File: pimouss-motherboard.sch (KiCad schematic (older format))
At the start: 0 parts

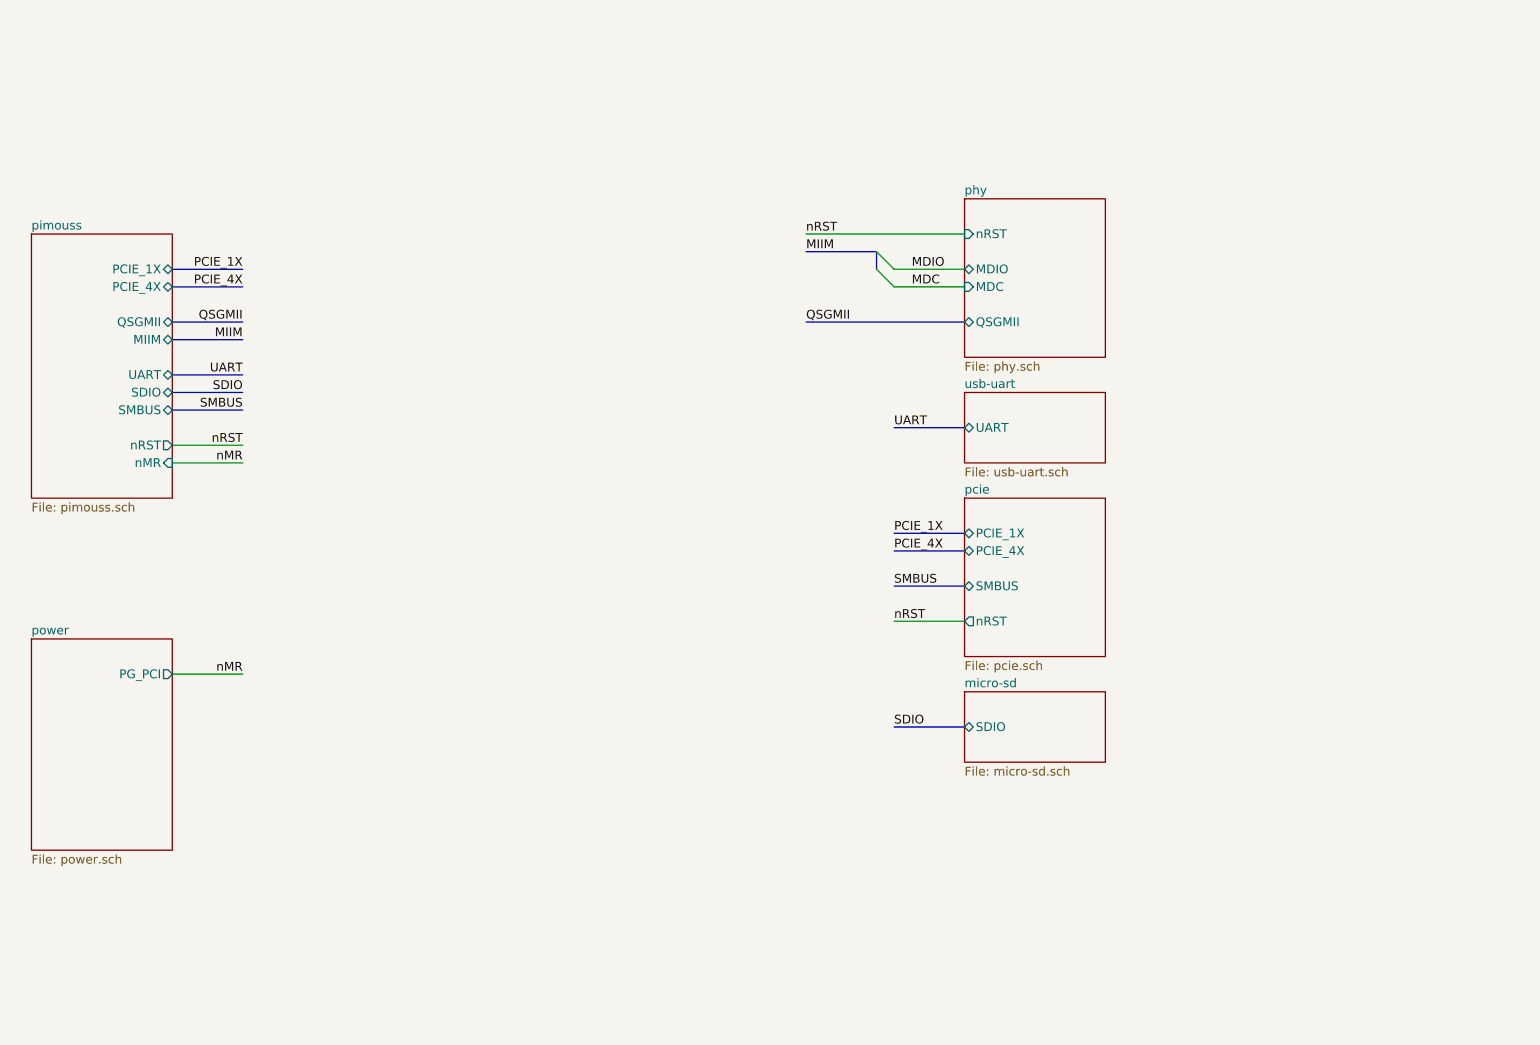
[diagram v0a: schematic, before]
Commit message: sch: Move PHY blocks to main page
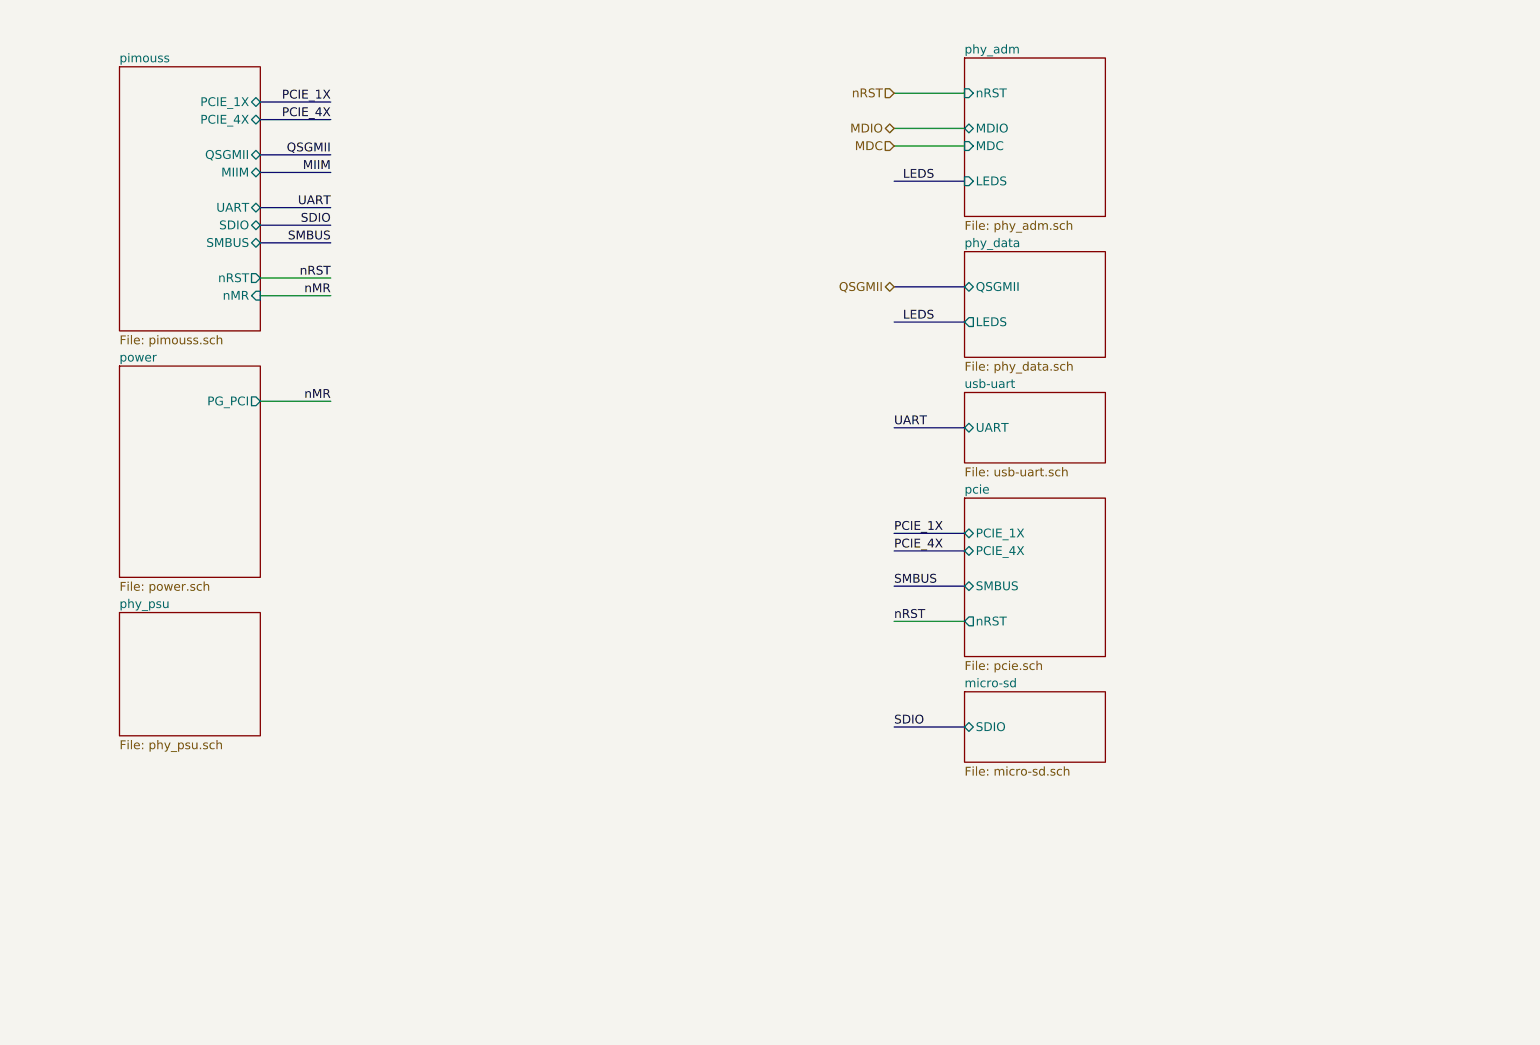
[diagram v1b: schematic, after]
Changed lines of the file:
@@
 $Descr A4 11693 8268
 encoding utf-8
-Sheet 1 13
+Sheet 1 12
 Title "Global motherboard interconnections"
 Date "2019-03-19"
@@
 $EndDescr
 $Sheet
-S 2100 2400 800  1500
+S 2600 1450 800  1500
 U 5CE77C37
 F0 "pimouss" 50
 F1 "pimouss.sch" 50
-F2 "PCIE_1X" B R 2900 2600 50
-F3 "PCIE_4X" B R 2900 2700 50
-F4 "QSGMII" B R 2900 2900 50
-F5 "MIIM" B R 2900 3000 50
-F6 "UART" B R 2900 3200 50
-F7 "SDIO" B R 2900 3300 50
-F8 "SMBUS" B R 2900 3400 50
-F9 "nRST" O R 2900 3600 50
-F10 "nMR" I R 2900 3700 50
-$EndSheet
-$Sheet
-S 7400 2200 800  900
-U 5C7D0D1E
-F0 "phy" 50
-F1 "phy.sch" 50
-F2 "nRST" I L 7400 2400 50
-F3 "MDIO" B L 7400 2600 50
-F4 "MDC" I L 7400 2700 50
-F5 "QSGMII" B L 7400 2900 50
+F2 "PCIE_1X" B R 3400 1650 50
+F3 "PCIE_4X" B R 3400 1750 50
+F4 "QSGMII" B R 3400 1950 50
+F5 "MIIM" B R 3400 2050 50
+F6 "UART" B R 3400 2250 50
+F7 "SDIO" B R 3400 2350 50
+F8 "SMBUS" B R 3400 2450 50
+F9 "nRST" O R 3400 2650 50
+F10 "nMR" I R 3400 2750 50
 $EndSheet
 Wire Bus Line
-	2900 2600 3300 2600
-Text Label 3300 2600 2    50   ~ 0
+	3400 1650 3800 1650
+Text Label 3800 1650 2    50   ~ 0
 PCIE_1X
 Wire Bus Line
-	2900 2700 3300 2700
-Text Label 3300 2700 2    50   ~ 0
+	3400 1750 3800 1750
+Text Label 3800 1750 2    50   ~ 0
 PCIE_4X
 Wire Bus Line
-	2900 2900 3300 2900
-Text Label 3300 2900 2    50   ~ 0
+	3400 1950 3800 1950
+Text Label 3800 1950 2    50   ~ 0
 QSGMII
 Wire Bus Line
-	3300 3000 2900 3000
-Text Label 3300 3000 2    50   ~ 0
+	3800 2050 3400 2050
+Text Label 3800 2050 2    50   ~ 0
 MIIM
 Wire Bus Line
-	2900 3200 3300 3200
-Text Label 3300 3200 2    50   ~ 0
+	3400 2250 3800 2250
+Text Label 3800 2250 2    50   ~ 0
 UART
 Wire Bus Line
-	2900 3300 3300 3300
-Text Label 3300 3300 2    50   ~ 0
+	3400 2350 3800 2350
+Text Label 3800 2350 2    50   ~ 0
 SDIO
 Wire Bus Line
-	2900 3400 3300 3400
-Text Label 3300 3400 2    50   ~ 0
+	3400 2450 3800 2450
+Text Label 3800 2450 2    50   ~ 0
 SMBUS
 Wire Wire Line
-	3300 3600 2900 3600
+	3800 2650 3400 2650
 Wire Wire Line
-	3300 3700 2900 3700
-Text Label 3300 3600 2    50   ~ 0
+	3800 2750 3400 2750
+Text Label 3800 2650 2    50   ~ 0
 nRST
-Text Label 3300 3700 2    50   ~ 0
+Text Label 3800 2750 2    50   ~ 0
 nMR
-Wire Wire Line
-	6500 2400 7400 2400
-Text Label 6500 2400 0    50   ~ 0
-nRST
-Wire Bus Line
-	7400 2900 6500 2900
-Text Label 6500 2900 0    50   ~ 0
-QSGMII
-Text Label 7100 2600 0    50   ~ 0
-MDIO
-Wire Bus Line
-	6900 2600 6900 2500
-Entry Wire Line
-	6900 2600 7000 2700
-Entry Wire Line
-	6900 2500 7000 2600
-Wire Bus Line
-	6500 2500 6900 2500
-Text Label 6500 2500 0    50   ~ 0
-MIIM
 $Sheet
 S 7400 3900 800  900
@@
 Text Label 7000 3500 0    50   ~ 0
 UART
-Text Label 7100 2700 0    50   ~ 0
-MDC
-Wire Wire Line
-	7000 2700 7400 2700
-Wire Wire Line
-	7000 2600 7400 2600
 $Sheet
 S 7400 5000 800  400
@@
 SDIO
 $Sheet
-S 2100 4700 800  1200
+S 7400 2500 800  600
+U 5D05A5DB
+F0 "phy_data" 50
+F1 "phy_data.sch" 50
+F2 "QSGMII" B L 7400 2700 50
+F3 "LEDS" O L 7400 2900 50
+$EndSheet
+$Sheet
+S 7400 1400 800  900
+U 5D05A5E1
+F0 "phy_adm" 50
+F1 "phy_adm.sch" 50
+F2 "nRST" I L 7400 1600 50
+F3 "MDIO" B L 7400 1800 50
+F4 "MDC" I L 7400 1900 50
+F5 "LEDS" I L 7400 2100 50
+$EndSheet
+Text HLabel 7000 1600 0    50   Input ~ 0
+nRST
+Wire Wire Line
+	7000 1600 7400 1600
+Text HLabel 7000 1800 0    50   BiDi ~ 0
+MDIO
+Text HLabel 7000 1900 0    50   Input ~ 0
+MDC
+Wire Wire Line
+	7000 1800 7400 1800
+Wire Wire Line
+	7400 1900 7000 1900
+Wire Bus Line
+	7400 2100 7000 2100
+Wire Bus Line
+	7400 2900 7000 2900
+Text Label 7050 2100 0    50   ~ 0
+LEDS
+Text Label 7050 2900 0    50   ~ 0
+LEDS
+Text HLabel 7000 2700 0    50   BiDi ~ 0
+QSGMII
+Wire Bus Line
+	7000 2700 7400 2700
+$Sheet
+S 2600 4550 800  700
+U 5D05A5E3
+F0 "phy_psu" 50
+F1 "phy_psu.sch" 50
+$EndSheet
+Text Label 3800 3350 2    50   ~ 0
+nMR
+Wire Wire Line
+	3800 3350 3400 3350
+$Sheet
+S 2600 3150 800  1200
 U 5D0C4621
 F0 "power" 50
 F1 "power.sch" 50
-F2 "PG_PCI" O R 2900 4900 50
+F2 "PG_PCI" O R 3400 3350 50
 $EndSheet
-Wire Wire Line
-	3300 4900 2900 4900
-Text Label 3300 4900 2    50   ~ 0
-nMR
 $EndSCHEMATC

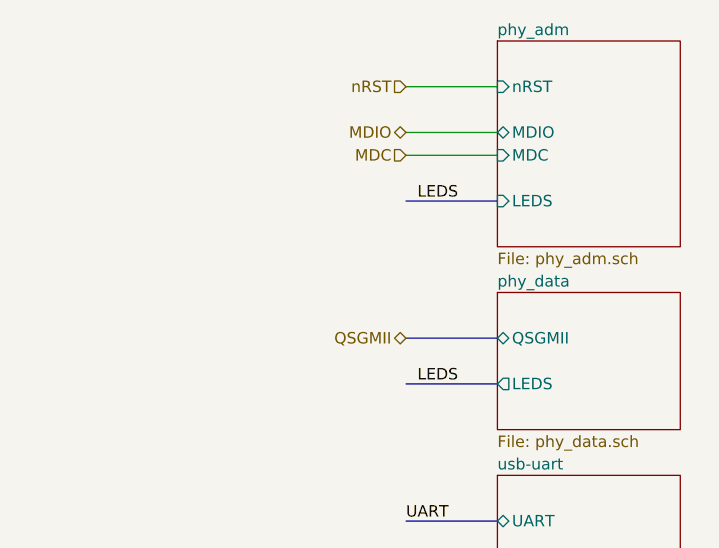
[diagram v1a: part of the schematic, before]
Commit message: sch: Misc fixes
- add missing NC on PCIe switch
- fix incorrect cap values on PCIe supply
- fix main schematic interco labels
- fix PHY JTAG signal name
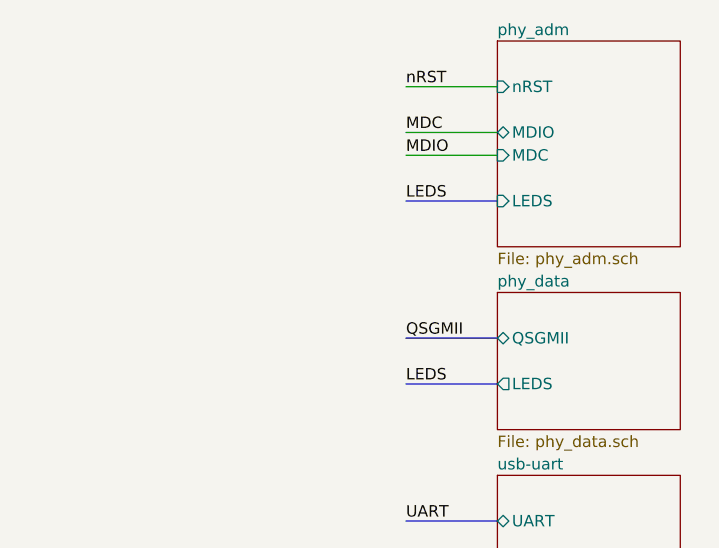
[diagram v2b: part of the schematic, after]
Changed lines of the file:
@@
 F5 "LEDS" I L 7400 2100 50
 $EndSheet
-Text HLabel 7000 1600 0    50   Input ~ 0
-nRST
 Wire Wire Line
 	7000 1600 7400 1600
-Text HLabel 7000 1800 0    50   BiDi ~ 0
-MDIO
-Text HLabel 7000 1900 0    50   Input ~ 0
-MDC
-Wire Wire Line
-	7000 1800 7400 1800
-Wire Wire Line
-	7400 1900 7000 1900
 Wire Bus Line
 	7400 2100 7000 2100
 Wire Bus Line
 	7400 2900 7000 2900
-Text Label 7050 2100 0    50   ~ 0
+Text Label 7000 2100 0    50   ~ 0
 LEDS
-Text Label 7050 2900 0    50   ~ 0
+Text Label 7000 2900 0    50   ~ 0
 LEDS
-Text HLabel 7000 2700 0    50   BiDi ~ 0
-QSGMII
 Wire Bus Line
 	7000 2700 7400 2700
@@
 F2 "PG_PCI" O R 3400 3350 50
 $EndSheet
+Text Label 7000 2700 0    50   ~ 0
+QSGMII
+Wire Wire Line
+	7000 1800 7400 1800
+Wire Wire Line
+	7000 1900 7400 1900
+Text Label 7000 1800 0    50   ~ 0
+MDC
+Text Label 7000 1900 0    50   ~ 0
+MDIO
+Text Label 7000 1600 0    50   ~ 0
+nRST
 $EndSCHEMATC

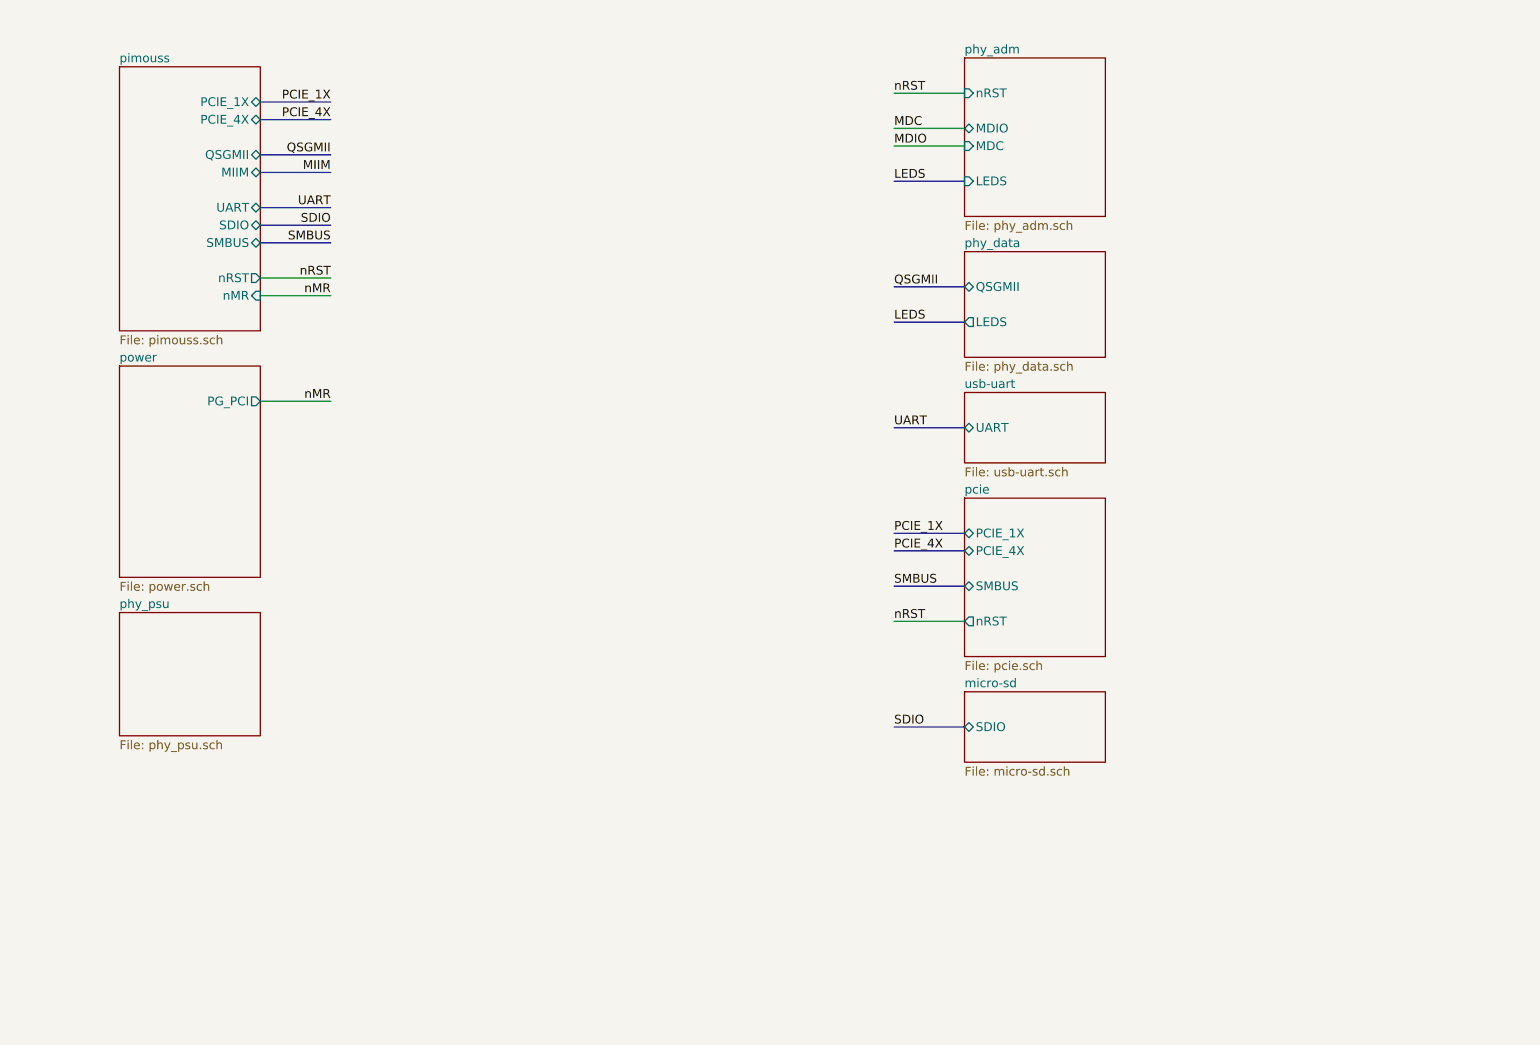
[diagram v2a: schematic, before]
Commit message: sch: Remove ALL busses since kicad's support is broken
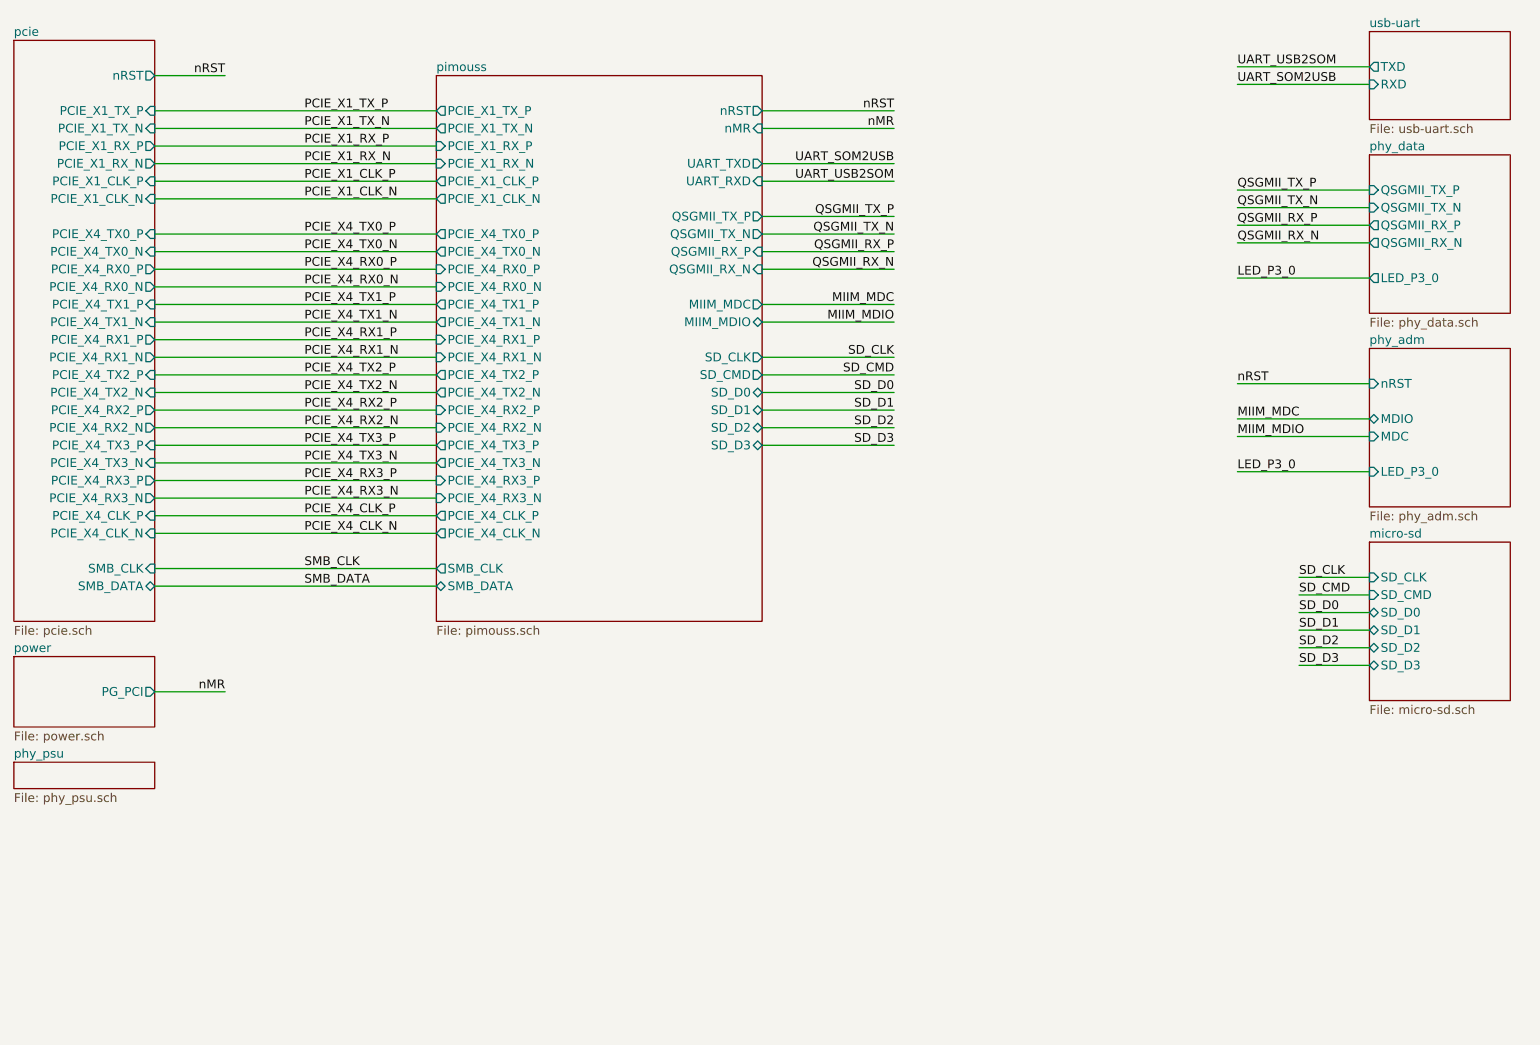
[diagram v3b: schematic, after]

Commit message: lib, sch: Misc changes to make ERC happy
- add resistors to PCIe switch GPIOs
- add NC flags on PHY unused LED outputs
- add dummy supply on Earth PSU
- add dummy supply on PHY ref clock's VCC
- LTC3633: deduplicate SW1/2 outputs
- ILS8033: deduplicate LX1/2 and PGND1/2 outputs
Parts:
- added DS?: DummySupply, symbol pimouss-motherboard:DummySupply
- added R?: 1M, symbol Device:R_Small
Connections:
- new net Earth: DS?.~ (Dummy), R?.1
- new net GND: R?.2
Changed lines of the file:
@@
 Text Label 8950 3750 0    50   ~ 0
 LED_P3_0
+$Comp
+L power:GND #PWR?
+U 1 1 5E474FB1
+P 4000 6700
+F 0 "#PWR?" H 4000 6450 50  0001 C CNN
+F 1 "GND" H 4005 6527 50  0000 C CNN
+F 2 "" H 4000 6700 50  0001 C CNN
+F 3 "" H 4000 6700 50  0001 C CNN
+	1    4000 6700
+	1    0    0    -1
+$EndComp
+$Comp
+L power:Earth #PWR?
+U 1 1 5E475AA8
+P 4400 6700
+F 0 "#PWR?" H 4400 6450 50  0001 C CNN
+F 1 "Earth" H 4400 6550 50  0001 C CNN
+F 2 "" H 4400 6700 50  0001 C CNN
+F 3 "~" H 4400 6700 50  0001 C CNN
+	1    4400 6700
+	1    0    0    -1
+$EndComp
+$Comp
+L pimouss-motherboard:DummySupply DS?
+U 1 1 5E47640A
+P 4400 6600
+F 0 "DS?" H 4400 6600 50  0001 C CNN
+F 1 "DummySupply" H 4400 6600 50  0001 C CNN
+F 2 "" H 4400 6600 50  0001 C CNN
+F 3 "" H 4400 6600 50  0001 C CNN
+	1    4400 6600
+	1    0    0    -1
+$EndComp
+$Comp
+L Device:R_Small R?
+U 1 1 5E476DB3
+P 4200 6600
+F 0 "R?" V 4004 6600 50  0000 C CNN
+F 1 "1M" V 4095 6600 50  0000 C CNN
+F 2 "" H 4200 6600 50  0001 C CNN
+F 3 "~" H 4200 6600 50  0001 C CNN
+	1    4200 6600
+	0    1    1    0
+$EndComp
+Wire Wire Line
+	4000 6700 4000 6600
+Wire Wire Line
+	4000 6600 4100 6600
+Wire Wire Line
+	4300 6600 4400 6600
+Wire Wire Line
+	4400 6600 4400 6700
+Connection ~ 4400 6600
 $EndSCHEMATC
